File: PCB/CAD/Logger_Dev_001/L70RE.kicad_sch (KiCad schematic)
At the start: 17 parts, among them J1 Conn_Coaxial, Q2 MMBT3904, U1 L76-M33

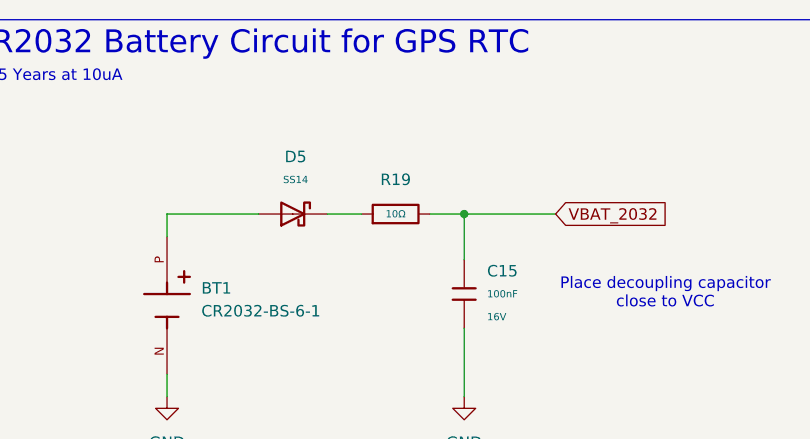
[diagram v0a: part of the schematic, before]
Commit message: ECR Update to schematic
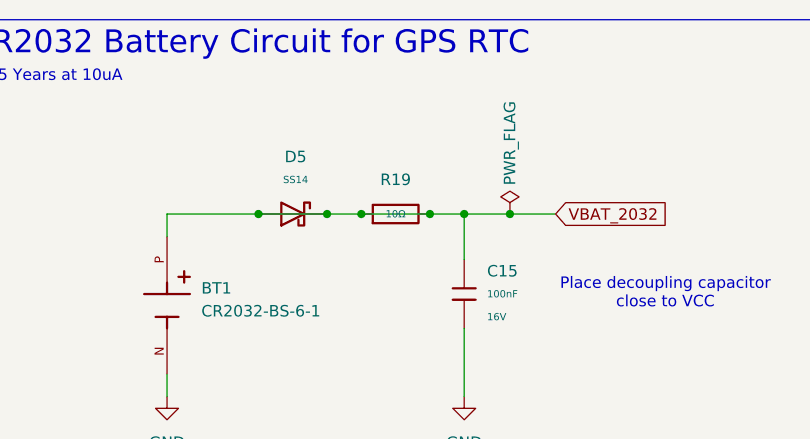
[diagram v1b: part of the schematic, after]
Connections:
- net VBAT_2032: now also BT1.P, D5.1, D5.2, R19.1
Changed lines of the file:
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@@
 	)
 	(junction
+		(at 73.66 36.83)
+		(diameter 0)
+		(color 0 0 0 0)
+	)
+	(junction
 		(at 82.55 119.38)
 		(diameter 0)
@@
 	)
 	(junction
+		(at 54.61 36.83)
+		(diameter 0)
+		(color 0 0 0 0)
+	)
+	(junction
 		(at 250.19 140.97)
 		(diameter 0)
@@
 	)
 	(junction
+		(at 66.04 36.83)
+		(diameter 0)
+		(color 0 0 0 0)
+	)
+	(junction
 		(at 158.75 116.84)
 		(diameter 0)
 		(color 0 0 0 0)
 	)
+	(junction
+		(at 82.55 36.83)
+		(diameter 0)
+		(color 0 0 0 0)
+	)
+	(junction
+		(at 62.23 36.83)
+		(diameter 0)
+		(color 0 0 0 0)
+	)
 	(no_connect
 		(at 161.29 106.68)
@@
 	(wire
 		(pts
+			(xy 77.47 36.83) (xy 73.66 36.83)
+		)
+		(stroke
+			(width 0)
+			(type default)
+		)
+	)
+	(wire
+		(pts
 			(xy 83.82 106.68) (xy 87.63 106.68)
 		)
@@
 	(wire
 		(pts
-			(xy 73.66 36.83) (xy 77.47 36.83)
+			(xy 73.66 36.83) (xy 66.04 36.83)
 		)
 		(stroke
@@
 	(wire
 		(pts
+			(xy 62.23 36.83) (xy 54.61 36.83)
+		)
+		(stroke
+			(width 0)
+			(type default)
+		)
+	)
+	(wire
+		(pts
 			(xy 166.37 128.27) (xy 157.48 128.27)
 		)
@@
 	(wire
 		(pts
+			(xy 82.55 36.83) (xy 87.63 36.83)
+		)
+		(stroke
+			(width 0)
+			(type default)
+		)
+	)
+	(wire
+		(pts
 			(xy 190.5 121.92) (xy 190.5 124.46)
 		)
@@
 	(wire
 		(pts
-			(xy 77.47 36.83) (xy 87.63 36.83)
+			(xy 77.47 36.83) (xy 82.55 36.83)
 		)
 		(stroke
@@
 					(unit 1)
 				)
+			)
+		)
+	)
+	(symbol
+		(lib_id "power:PWR_FLAG")
+		(at 82.55 36.83 0)
+		(unit 1)
+		(exclude_from_sim no)
+		(in_bom yes)
+		(on_board yes)
+		(dnp no)
+		(property "Reference" "#FLG04"
+			(at 82.55 34.925 0)
+			(effects
+				(font
+					(size 1.27 1.27)
+				)
+				(hide yes)
+			)
+		)
+		(property "Value" "PWR_FLAG"
+			(at 82.55 28.956 90)
+			(effects
+				(font
+					(size 1.27 1.27)
+				)
+			)
+		)
+		(property "Footprint" ""
+			(at 82.55 36.83 0)
+			(effects
+				(font
+					(size 1.27 1.27)
+				)
+				(hide yes)
+			)
+		)
+		(property "Datasheet" "~"
+			(at 82.55 36.83 0)
+			(effects
+				(font
+					(size 1.27 1.27)
+				)
+				(hide yes)
+			)
+		)
+		(property "Description" "Special symbol for telling ERC where power comes from"
+			(at 82.55 36.83 0)
+			(effects
+				(font
+					(size 1.27 1.27)
+				)
+				(hide yes)
+			)
+		)
+		(pin "1"
+		)
+		(instances
+			(project "Logger_Dev_001"
+				(path "/9546b831-c7ee-4f40-8993-5fd5a38d4078/b37dc544-49d2-4960-bf8e-49b471c058c3"
+					(reference "#FLG04")
+					(unit 1)
+				)

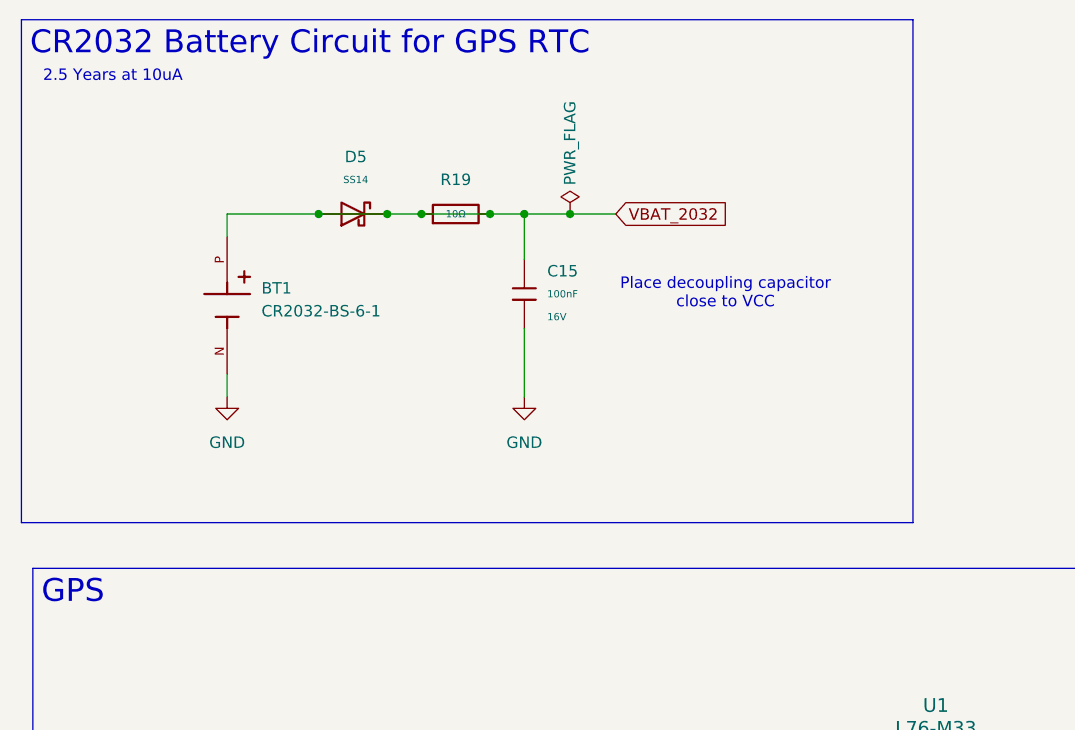
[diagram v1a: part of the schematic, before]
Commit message: Update via size to reduce cost
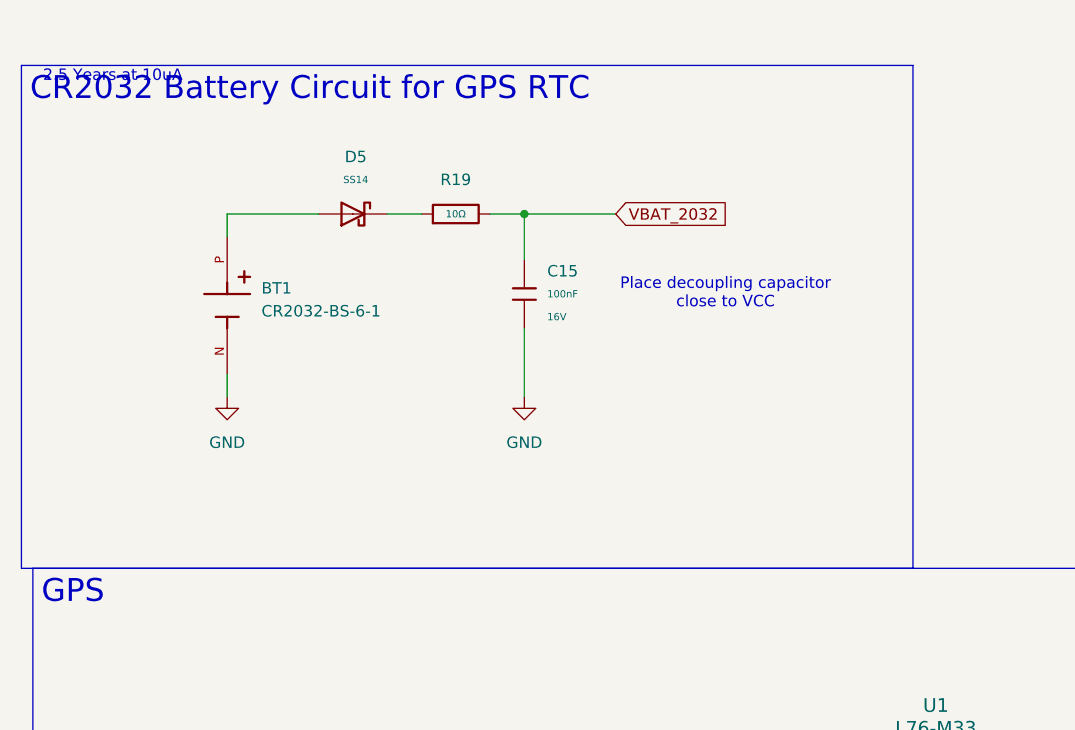
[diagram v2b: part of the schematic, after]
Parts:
- BT1: LCSC (none) -> C70377
- J1: LCSC (none) -> C7498154
- TP13, TP14: now left out of the parts list
- U1: LCSC (none) -> C2916232
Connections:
- net VBAT_2032: no longer BT1.P, D5.1, D5.2, R19.1
- new net: D5.1, R19.1
- new net: BT1.P, D5.2
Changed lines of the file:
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@@
 	(text_box "CR2032 Battery Circuit for GPS RTC\n"
 		(exclude_from_sim no)
-		(at 21.59 15.24 0)
+		(at 21.59 20.32 0)
 		(size 99.06 55.88)
 		(margins 0.9525 0.9525 0.9525 0.9525)
@@
 	)
 	(junction
-		(at 73.66 36.83)
-		(diameter 0)
-		(color 0 0 0 0)
-	)
-	(junction
 		(at 82.55 119.38)
 		(diameter 0)
@@
 	)
 	(junction
-		(at 54.61 36.83)
-		(diameter 0)
-		(color 0 0 0 0)
-	)
-	(junction
 		(at 250.19 140.97)
 		(diameter 0)
@@
 	)
 	(junction
-		(at 66.04 36.83)
-		(diameter 0)
-		(color 0 0 0 0)
-	)
-	(junction
 		(at 158.75 116.84)
 		(diameter 0)
 		(color 0 0 0 0)
 	)
-	(junction
-		(at 82.55 36.83)
-		(diameter 0)
-		(color 0 0 0 0)
-	)
-	(junction
-		(at 62.23 36.83)
-		(diameter 0)
-		(color 0 0 0 0)
-	)
 	(no_connect
 		(at 161.29 106.68)
@@
 	(wire
 		(pts
-			(xy 73.66 36.83) (xy 66.04 36.83)
-		)
-		(stroke
-			(width 0)
-			(type default)
-		)
-	)
-	(wire
-		(pts
 			(xy 157.48 128.27) (xy 157.48 132.08)
 		)
@@
 	(wire
 		(pts
-			(xy 62.23 36.83) (xy 54.61 36.83)
-		)
-		(stroke
-			(width 0)
-			(type default)
-		)
-	)
-	(wire
-		(pts
 			(xy 166.37 128.27) (xy 157.48 128.27)
 		)
@@
 	(wire
 		(pts
-			(xy 62.23 36.83) (xy 66.04 36.83)
+			(xy 77.47 49.53) (xy 77.47 57.15)
 		)
 		(stroke
@@
 	(wire
 		(pts
-			(xy 77.47 49.53) (xy 77.47 57.15)
+			(xy 157.48 139.7) (xy 157.48 143.51)
 		)
 		(stroke
@@
 	(wire
 		(pts
-			(xy 157.48 139.7) (xy 157.48 143.51)
+			(xy 44.45 36.83) (xy 54.61 36.83)
 		)
 		(stroke
@@
 	(wire
 		(pts
-			(xy 44.45 36.83) (xy 54.61 36.83)
+			(xy 190.5 116.84) (xy 190.5 121.92)
 		)
 		(stroke
@@
 	(wire
 		(pts
-			(xy 190.5 116.84) (xy 190.5 121.92)
+			(xy 177.8 119.38) (xy 194.31 119.38)
 		)
 		(stroke
@@
 	(wire
 		(pts
-			(xy 177.8 119.38) (xy 194.31 119.38)
+			(xy 166.37 128.27) (xy 166.37 129.54)
 		)
 		(stroke
@@
 	(wire
 		(pts
-			(xy 166.37 128.27) (xy 166.37 129.54)
+			(xy 77.47 36.83) (xy 87.63 36.83)
 		)
 		(stroke
@@
 	(wire
 		(pts
-			(xy 82.55 36.83) (xy 87.63 36.83)
+			(xy 62.23 36.83) (xy 66.04 36.83)
 		)
 		(stroke
@@
 	(wire
 		(pts
-			(xy 77.47 36.83) (xy 82.55 36.83)
-		)
-		(stroke
-			(width 0)
-			(type default)
-		)
-	)
-	(wire
-		(pts
 			(xy 82.55 125.73) (xy 82.55 119.38)
 		)
@@
 			)
 		)
-		(property "Description" ""
+		(property "Description" "-165dBm -40℃~+85℃ 2.8V~4.3V SMD-18P GNSS Modules ROHS"
+			(at 87.63 101.6 0)
+			(effects
+				(font
+					(size 1.27 1.27)
+				)
+				(hide yes)
+			)
+		)
+		(property "LCSC" "C2916232"
 			(at 87.63 101.6 0)
 			(effects
@@
 			)
 		)
-		(property "Datasheet" "~"
+		(property "Datasheet" "https://jlcpcb.com/api/file/downloadByFileSystemAccessId/8600772178468225024"
 			(at 199.39 119.38 0)
 			(effects
@@
 			)
 		)
-		(property "Description" "coaxial connector (BNC, SMA, SMB, SMC, Cinch/RCA, LEMO, ...)"
+		(property "Description" "-45℃~+80℃ 1 14.6mm 4.65mm 50Ω 6GHz Board Side Inner Bore Plugin Coaxial Connectors (RF) ROHS"
+			(at 199.39 119.38 0)
+			(effects
+				(font
+					(size 1.27 1.27)
+				)
+				(hide yes)
+			)
+		)
+		(property "LCSC" "C7498154"
 			(at 199.39 119.38 0)
 			(effects
@@
 		(unit 1)
 		(exclude_from_sim no)
-		(in_bom yes)
+		(in_bom no)
 		(on_board yes)
 		(dnp no)
@@
 			)
 		)
-		(property "Datasheet" ""
+		(property "Datasheet" "https://jlcpcb.com/api/file/downloadByFileSystemAccessId/8588884037066350592"
 			(at 44.45 46.99 0)
 			(effects
@@
 			)
 		)
-		(property "Description" ""
+		(property "Description" "Battery Holder CR2032 SMD Button And Strip Battery Connector ROHS"
 			(at 44.45 46.99 0)
 			(effects
@@
 			)
 		)
+		(property "LCSC" "C70377"
+			(at 44.45 46.99 90)
+			(effects
+				(font
+					(size 1.27 1.27)
+				)
+				(hide yes)
+			)
+		)
 		(pin "P"
 		)
@@
 		(unit 1)
 		(exclude_from_sim no)
-		(in_bom yes)
+		(in_bom no)
 		(on_board yes)
 		(dnp no)
@@
 					(unit 1)
 				)
-			)
-		)
-	)
-	(symbol
-		(lib_id "power:PWR_FLAG")
-		(at 82.55 36.83 0)
-		(unit 1)
-		(exclude_from_sim no)
-		(in_bom yes)
-		(on_board yes)
-		(dnp no)
-		(property "Reference" "#FLG04"
-			(at 82.55 34.925 0)
-			(effects
-				(font
-					(size 1.27 1.27)
-				)
-				(hide yes)
-			)
-		)
-		(property "Value" "PWR_FLAG"
-			(at 82.55 28.956 90)
-			(effects
-				(font
-					(size 1.27 1.27)
-				)
-			)
-		)
-		(property "Footprint" ""
-			(at 82.55 36.83 0)
-			(effects
-				(font
-					(size 1.27 1.27)
-				)
-				(hide yes)
-			)
-		)
-		(property "Datasheet" "~"
-			(at 82.55 36.83 0)
-			(effects
-				(font
-					(size 1.27 1.27)
-				)
-				(hide yes)
-			)
-		)
-		(property "Description" "Special symbol for telling ERC where power comes from"
-			(at 82.55 36.83 0)
-			(effects
-				(font
-					(size 1.27 1.27)
-				)
-				(hide yes)
-			)
-		)
-		(pin "1"
-		)
-		(instances
-			(project "Logger_Dev_001"
-				(path "/9546b831-c7ee-4f40-8993-5fd5a38d4078/b37dc544-49d2-4960-bf8e-49b471c058c3"
-					(reference "#FLG04")
-					(unit 1)
-				)

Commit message: Clean PCB and Project
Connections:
- net VBAT_2032 renamed PWR_FLAG
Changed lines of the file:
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@@
 	(text "2.5 Years at 10uA"
 		(exclude_from_sim no)
-		(at 31.75 21.59 0)
+		(at 31.75 26.67 0)
 		(effects
 			(font
@@
 	)
 	(junction
+		(at 81.28 36.83)
+		(diameter 0)
+		(color 0 0 0 0)
+	)
+	(junction
 		(at 82.55 119.38)
 		(diameter 0)
@@
 	(wire
 		(pts
-			(xy 77.47 36.83) (xy 87.63 36.83)
+			(xy 77.47 36.83) (xy 81.28 36.83)
 		)
 		(stroke
@@
 	(wire
 		(pts
+			(xy 81.28 36.83) (xy 87.63 36.83)
+		)
+		(stroke
+			(width 0)
+			(type default)
+		)
+	)
+	(wire
+		(pts
 			(xy 44.45 54.61) (xy 44.45 57.15)
 		)
@@
 					(unit 1)
 				)
+			)
+		)
+	)
+	(symbol
+		(lib_name "PWR_FLAG_1")
+		(lib_id "power:PWR_FLAG")
+		(at 81.28 36.83 0)
+		(unit 1)
+		(exclude_from_sim no)
+		(in_bom yes)
+		(on_board yes)
+		(dnp no)
+		(property "Reference" "#FLG04"
+			(at 81.28 34.925 0)
+			(effects
+				(font
+					(size 1.27 1.27)
+				)
+				(hide yes)
+			)
+		)
+		(property "Value" "PWR_FLAG"
+			(at 81.28 28.956 90)
+			(effects
+				(font
+					(size 1.27 1.27)
+				)
+			)
+		)
+		(property "Footprint" ""
+			(at 81.28 36.83 0)
+			(effects
+				(font
+					(size 1.27 1.27)
+				)
+				(hide yes)
+			)
+		)
+		(property "Datasheet" "~"
+			(at 81.28 36.83 0)
+			(effects
+				(font
+					(size 1.27 1.27)
+				)
+				(hide yes)
+			)
+		)
+		(property "Description" "Special symbol for telling ERC where power comes from"
+			(at 81.28 36.83 0)
+			(effects
+				(font
+					(size 1.27 1.27)
+				)
+				(hide yes)
+			)
+		)
+		(pin "1"
+		)
+		(instances
+			(project "Logger_Dev_001"
+				(path "/9546b831-c7ee-4f40-8993-5fd5a38d4078/b37dc544-49d2-4960-bf8e-49b471c058c3"
+					(reference "#FLG04")
+					(unit 1)
+				)
